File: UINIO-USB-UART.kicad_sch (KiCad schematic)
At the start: 32 parts, among them J1 Conn_01x08_Male, J2 Conn_01x04_Male, J3 Conn_01x07_Male, J4 Conn_01x06_Male, J5 Conn_01x04_Male, J6 Conn_01x07_Male, J7 Conn_01x03_Male, U1 CP2102, U2 CH343P

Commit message: Update PCB.
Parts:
- added R10, R7, R8, R9: 5.1K, Resistor_SMD:R_0603_1608Metric, symbol Device:R
- C3: value 0.1uF -> 4.7uF
- C4: value 4.7uF -> 0.1uF
- D1: value Green LED -> LED Red
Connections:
- net CH343_VDD_3.3V: now also J6.2 (Pin_2), R1.2; no longer J6.1 (Pin_1)
- net CH343_VDD_5V: now also J4.2 (Pin_2); no longer J4.1 (Pin_1), R1.2
- net CP2102_DTR: now also J2.1 (Pin_1); no longer J2.4 (Pin_4)
- net CP2102_RTS: now also J2.4 (Pin_4); no longer J2.1 (Pin_1)
- net CP2102_RXD: now also J2.2 (Pin_2); no longer J2.3 (Pin_3)
- net CP2102_TXD: now also J2.3 (Pin_3); no longer J2.2 (Pin_2)
- net CP2102_VDD_3.3V: now also J3.2 (Pin_2); no longer J3.1 (Pin_1)
- net CP2102_VDD_5V: now also J1.2 (Pin_2); no longer J1.1 (Pin_1)
- net GND: now also J1.1 (Pin_1), J3.1 (Pin_1), J4.1 (Pin_1), J6.1 (Pin_1), R10.1, R7.1, R8.1, R9.1; no longer J1.2 (Pin_2), J3.2 (Pin_2), J4.2 (Pin_2), J6.2 (Pin_2)
- net at USB2.A5 (CC1): now also R7.2
- net at USB2.B5 (CC2): now also R8.2
- net at USB1.A5 (CC1): now also R9.2
- net at USB1.B5 (CC2): now also R10.2
- no-connect marks 19 -> 15
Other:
- moved on the sheet: C6, D1, D4, F1, J2, R1, R4

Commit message: PCB Update.
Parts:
- D4: value Green LED -> LED Red
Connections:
- net CP2102_VDD_3.3V: now also R4.2
- net CP2102_VDD_5V: no longer R4.2
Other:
- moved on the sheet: C1, C2, C3, C4, D4, R4, U1

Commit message: Release UINIO-USB-UART version 3.0.0.
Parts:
- U2: footprint kicad_lceda:TQFN-16_L3.0-W3.0-P0.50-BL-EP1.7 -> Uinio:TQFN-16_L3.0-W3.0-P0.50-BL-EP1.7
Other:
- moved on the sheet: D1, R1
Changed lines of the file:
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@@
   (title_block
     (title "UINIO-USB-UART")
-    (date "2023-02-06")
+    (date "2023-02-07")
     (rev "Version 3.0.0")
     (company "电子技术博客 UinIO.com")
@@
     (stroke (width 0) (type default) (color 0 0 0 0))
   )
-  (wire (pts (xy 114.3 78.74) (xy 113.03 78.74))
+  (wire (pts (xy 114.3 76.2) (xy 113.03 76.2))
     (stroke (width 0) (type default) (color 0 0 0 0))
   )
@@
     (stroke (width 0.254) (type default) (color 0 0 0 0))
   )
-  (wire (pts (xy 121.92 69.85) (xy 121.92 66.04))
+  (wire (pts (xy 121.92 67.31) (xy 121.92 66.04))
     (stroke (width 0) (type default) (color 0 0 0 0))
   )
@@
     (stroke (width 0) (type default) (color 0 0 0 0))
   )
-  (wire (pts (xy 121.92 77.47) (xy 121.92 78.74))
+  (wire (pts (xy 121.92 74.93) (xy 121.92 76.2))
     (stroke (width 0) (type default) (color 0 0 0 0))
   )
@@
     (pin "2")
   )
-  (symbol (lib_id "Device:LED") (at 118.11 78.74 0) (unit 1)
-    (in_bom yes) (on_board yes)
-    (property "Reference" "D1" (id 0) (at 119.38 76.2 0)
-      (effects (font (size 1.27 1.27)) (justify right))
-    )
-    (property "Value" "LED Red" (id 1) (at 121.92 82.55 0)
-      (effects (font (size 1.27 1.27)) (justify right))
-    )
-    (property "Footprint" "LED_SMD:LED_0603_1608Metric" (id 2) (at 118.11 78.74 0)
-      (effects (font (size 1.27 1.27)) hide)
-    )
-    (property "Datasheet" "~" (id 3) (at 118.11 78.74 0)
+  (symbol (lib_id "Device:LED") (at 118.11 76.2 0) (unit 1)
+    (in_bom yes) (on_board yes)
+    (property "Reference" "D1" (id 0) (at 119.38 73.66 0)
+      (effects (font (size 1.27 1.27)) (justify right))
+    )
+    (property "Value" "LED Red" (id 1) (at 121.92 80.01 0)
+      (effects (font (size 1.27 1.27)) (justify right))
+    )
+    (property "Footprint" "LED_SMD:LED_0603_1608Metric" (id 2) (at 118.11 76.2 0)
+      (effects (font (size 1.27 1.27)) hide)
+    )
+    (property "Datasheet" "~" (id 3) (at 118.11 76.2 0)
       (effects (font (size 1.27 1.27)) hide)
     )
@@
     (pin "1")
   )
-  (symbol (lib_id "power:GND") (at 113.03 78.74 270) (mirror x) (unit 1)
-    (in_bom yes) (on_board yes)
-    (property "Reference" "#PWR02" (id 0) (at 106.68 78.74 0)
-      (effects (font (size 1.27 1.27)) hide)
-    )
-    (property "Value" "GND" (id 1) (at 110.49 78.74 90)
-      (effects (font (size 1.27 1.27)) (justify right))
-    )
-    (property "Footprint" "" (id 2) (at 113.03 78.74 0)
-      (effects (font (size 1.27 1.27)) hide)
-    )
-    (property "Datasheet" "" (id 3) (at 113.03 78.74 0)
-      (effects (font (size 1.27 1.27)) hide)
-    )
-    (pin "1")
-  )
-  (symbol (lib_id "Device:R") (at 121.92 73.66 0) (mirror x) (unit 1)
-    (in_bom yes) (on_board yes)
-    (property "Reference" "R1" (id 0) (at 124.46 73.66 90))
-    (property "Value" "2K" (id 1) (at 121.92 73.66 90))
-    (property "Footprint" "Resistor_SMD:R_0603_1608Metric" (id 2) (at 120.142 73.66 90)
-      (effects (font (size 1.27 1.27)) hide)
-    )
-    (property "Datasheet" "~" (id 3) (at 121.92 73.66 0)
+  (symbol (lib_id "power:GND") (at 113.03 76.2 270) (mirror x) (unit 1)
+    (in_bom yes) (on_board yes)
+    (property "Reference" "#PWR02" (id 0) (at 106.68 76.2 0)
+      (effects (font (size 1.27 1.27)) hide)
+    )
+    (property "Value" "GND" (id 1) (at 110.49 76.2 90)
+      (effects (font (size 1.27 1.27)) (justify right))
+    )
+    (property "Footprint" "" (id 2) (at 113.03 76.2 0)
+      (effects (font (size 1.27 1.27)) hide)
+    )
+    (property "Datasheet" "" (id 3) (at 113.03 76.2 0)
+      (effects (font (size 1.27 1.27)) hide)
+    )
+    (pin "1")
+  )
+  (symbol (lib_id "Device:R") (at 121.92 71.12 0) (mirror x) (unit 1)
+    (in_bom yes) (on_board yes)
+    (property "Reference" "R1" (id 0) (at 124.46 71.12 90))
+    (property "Value" "2K" (id 1) (at 121.92 71.12 90))
+    (property "Footprint" "Resistor_SMD:R_0603_1608Metric" (id 2) (at 120.142 71.12 90)
+      (effects (font (size 1.27 1.27)) hide)
+    )
+    (property "Datasheet" "~" (id 3) (at 121.92 71.12 0)
       (effects (font (size 1.27 1.27)) hide)
     )
@@
     (property "Reference" "U2" (id 0) (at 157.48 48.895 0))
     (property "Value" "CH343P" (id 1) (at 167.64 76.2 0))
-    (property "Footprint" "kicad_lceda:TQFN-16_L3.0-W3.0-P0.50-BL-EP1.7" (id 2) (at 170.18 76.2 0)
+    (property "Footprint" "Uinio:TQFN-16_L3.0-W3.0-P0.50-BL-EP1.7" (id 2) (at 170.18 76.2 0)
       (effects (font (size 1.27 1.27)) hide)
     )
@@
     )
     (path "/f9f0ec6d-076d-4cd3-8e74-63adeb9cbeee"
-      (reference "U2") (unit 1) (value "CH343P") (footprint "kicad_lceda:TQFN-16_L3.0-W3.0-P0.50-BL-EP1.7")
+      (reference "U2") (unit 1) (value "CH343P") (footprint "Uinio:TQFN-16_L3.0-W3.0-P0.50-BL-EP1.7")
     )
     (path "/89621895-1bc9-4914-8616-3f6600f3ea65"

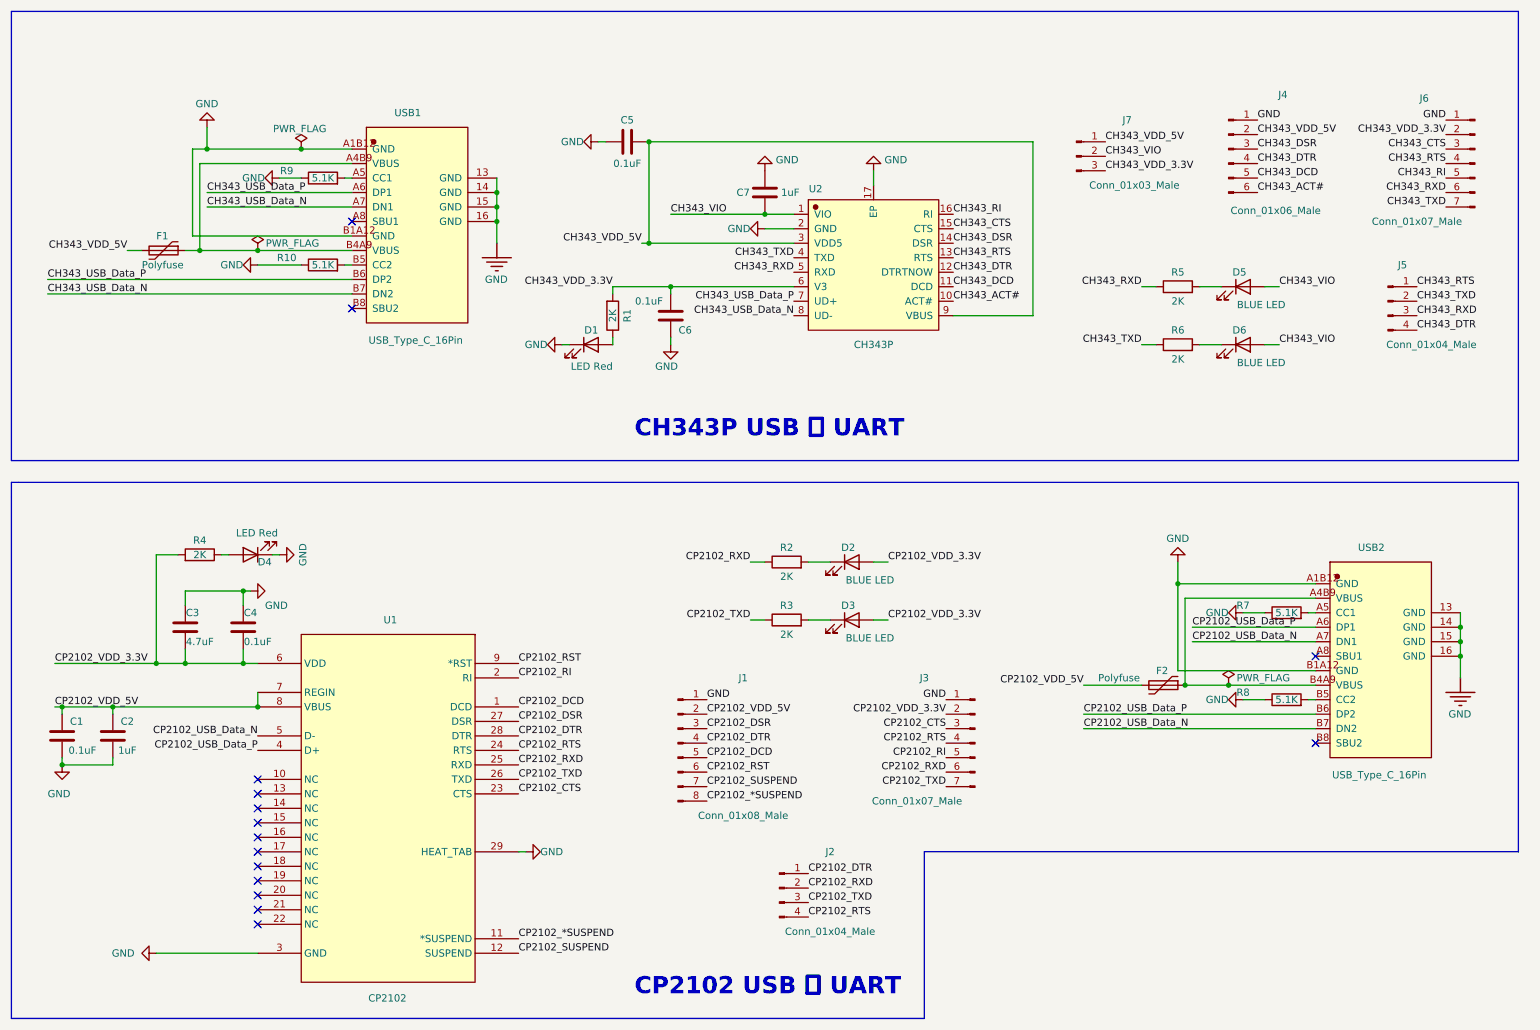
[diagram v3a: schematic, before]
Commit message: Prepare UINIO-USB-UART version 3.1.0
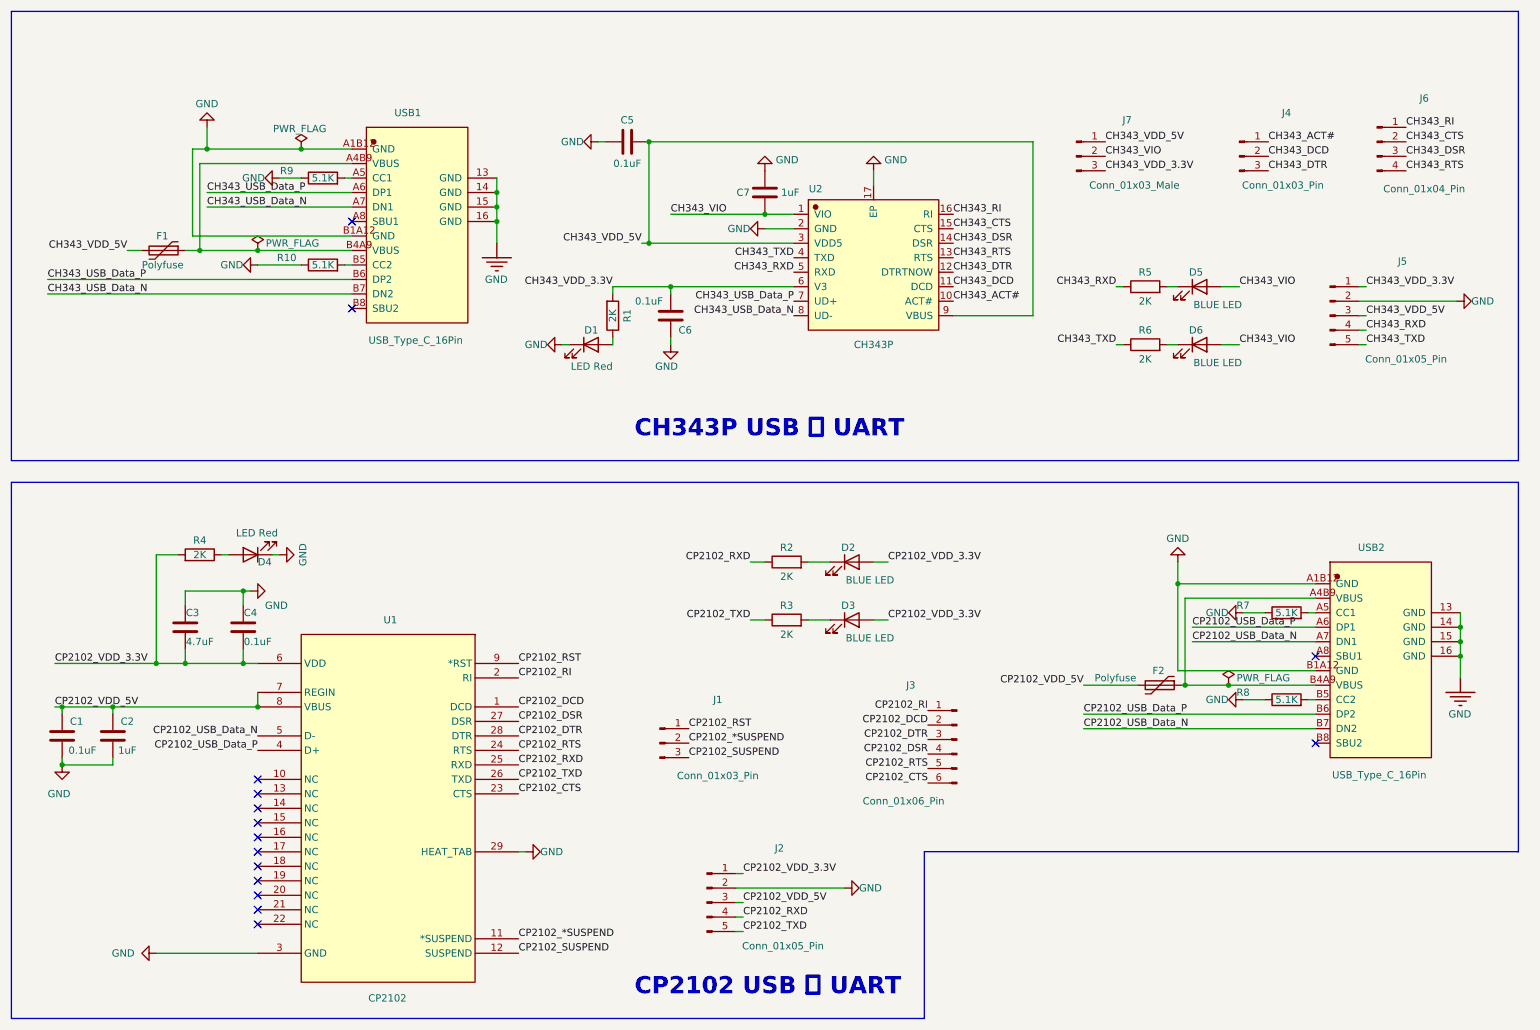
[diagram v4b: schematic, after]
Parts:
- removed J1: Conn_01x08_Male, Connector_PinHeader_2.54mm:PinHeader_1x08_P2.54mm_Vertical, symbol Connector:Conn_01x08_Male
- removed J2, J5: Conn_01x04_Male, Connector_PinHeader_2.54mm:PinHeader_1x04_P2.54mm_Vertical, symbol Connector:Conn_01x04_Male
- removed J3, J6: Conn_01x07_Male, Connector_PinHeader_2.54mm:PinHeader_1x07_P2.54mm_Vertical, symbol Connector:Conn_01x07_Male
- removed J4: Conn_01x06_Male, Connector_PinHeader_2.54mm:PinHeader_1x06_P2.54mm_Vertical, symbol Connector:Conn_01x06_Male
- added J1, J4: Conn_01x03_Pin, Connector_PinHeader_2.54mm:PinHeader_1x03_P2.54mm_Vertical, symbol Connector:Conn_01x03_Pin
- added J2, J5: Conn_01x05_Pin, Connector_PinHeader_2.54mm:PinHeader_1x05_P2.54mm_Vertical, symbol Connector:Conn_01x05_Pin
- added J3: Conn_01x06_Pin, Connector_PinHeader_2.54mm:PinHeader_1x06_P2.54mm_Vertical, symbol Connector:Conn_01x06_Pin
- added J6: Conn_01x04_Pin, Connector_PinHeader_2.54mm:PinHeader_1x04_P2.54mm_Vertical, symbol Connector:Conn_01x04_Pin
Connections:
- net CH343_ACT#: now also J4.1 (Pin_1)
- net CH343_CTS: now also J6.2 (Pin_2)
- net CH343_DCD: now also J4.2 (Pin_2)
- net CH343_DSR: now also J6.3 (Pin_3)
- net CH343_DTR: now also J4.3 (Pin_3)
- net CH343_RI: now also J6.1 (Pin_1)
- net CH343_RTS: now also J6.4 (Pin_4)
- net CH343_RXD: now also J5.4 (Pin_4)
- net CH343_TXD: now also J5.5 (Pin_5)
- net CH343_VDD_3.3V: now also J5.1 (Pin_1)
- net CH343_VDD_5V: now also J5.3 (Pin_3)
- net CP2102_*SUSPEND: now also J1.2 (Pin_2)
- net CP2102_CTS: now also J3.6 (Pin_6)
- net CP2102_DCD: now also J3.2 (Pin_2)
- net CP2102_DSR: now also J3.4 (Pin_4)
- net CP2102_DTR: now also J3.3 (Pin_3)
- net CP2102_RI: now also J3.1 (Pin_1)
- net CP2102_RST: now also J1.1 (Pin_1)
- net CP2102_RTS: now also J3.5 (Pin_5)
- net CP2102_RXD: now also J2.4 (Pin_4)
- net CP2102_SUSPEND: now also J1.3 (Pin_3)
- net CP2102_TXD: now also J2.5 (Pin_5)
- net CP2102_VDD_3.3V: now also J2.1 (Pin_1)
- net CP2102_VDD_5V: now also J2.3 (Pin_3)
- net GND: now also J2.2 (Pin_2), J5.2 (Pin_2)
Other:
- moved on the sheet: D5, D6, F2, R5, R6

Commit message: Prepare Version 3.2.0.
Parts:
- removed J7: Conn_01x03_Male, Connector_PinHeader_2.54mm:PinHeader_1x03_P2.54mm_Vertical, symbol Connector:Conn_01x03_Male
- added J7: Conn_01x03_Pin, Connector_PinHeader_2.54mm:PinHeader_1x03_P2.54mm_Vertical, symbol Connector:Conn_01x03_Pin
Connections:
- net CH343_RXD: now also J5.5 (Pin_5); no longer J5.4 (Pin_4)
- net CH343_TXD: now also J5.4 (Pin_4); no longer J5.5 (Pin_5)
- net CH343_VDD_3.3V: now also J5.3 (Pin_3), J7.3 (Pin_3); no longer J5.1 (Pin_1)
- net CH343_VDD_5V: now also J5.1 (Pin_1), J7.1 (Pin_1); no longer J5.3 (Pin_3)
- net CH343_VIO: now also J7.2 (Pin_2)
- net CP2102_VDD_3.3V: now also J2.3 (Pin_3); no longer J2.1 (Pin_1)
- net CP2102_VDD_5V: now also J2.1 (Pin_1); no longer J2.3 (Pin_3)
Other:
- moved on the sheet: F2, J1, J3, J4, J6, R5, R6

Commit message: Update PCB.
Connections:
- net CH343_VDD_3.3V: now also J7.1 (Pin_1); no longer J7.3 (Pin_3)
- net CH343_VDD_5V: now also J7.3 (Pin_3); no longer J7.1 (Pin_1)
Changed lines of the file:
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@@
     (effects (font (size 1.27 1.27)) (justify left bottom))
   )
-  (label "CH343_VDD_3.3V" (at 208.28 45.72 0) (fields_autoplaced)
+  (label "CH343_VDD_3.3V" (at 208.28 40.64 0) (fields_autoplaced)
     (effects (font (size 1.27 1.27)) (justify left bottom))
   )
@@
     (effects (font (size 1.27 1.27)) (justify left bottom))
   )
-  (label "CH343_VDD_5V" (at 208.28 40.64 0) (fields_autoplaced)
+  (label "CH343_VDD_5V" (at 208.28 45.72 0) (fields_autoplaced)
     (effects (font (size 1.27 1.27)) (justify left bottom))
   )

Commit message: Release UINIO-USB-UART version 3.2.0.
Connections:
- net CH343_VDD_3.3V: now also J5.2 (Pin_2); no longer J5.3 (Pin_3)
- net CP2102_VDD_3.3V: now also J2.2 (Pin_2); no longer J2.3 (Pin_3)
- net GND: now also J2.3 (Pin_3), J5.3 (Pin_3); no longer J2.2 (Pin_2), J5.2 (Pin_2)
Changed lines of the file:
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@@
   (title_block
     (title "UINIO-USB-UART")
-    (date "2023-06-26")
+    (date "2023-06-27")
     (rev "Version 3.2.0")
     (company "电子技术博客 UinIO.com")
@@
     (stroke (width 0) (type default))
   )
-  (wire (pts (xy 143.51 173.99) (xy 144.78 173.99))
+  (wire (pts (xy 143.51 171.45) (xy 144.78 171.45))
     (stroke (width 0) (type default))
   )
@@
     (stroke (width 0) (type default))
   )
-  (wire (pts (xy 252.73 68.58) (xy 270.51 68.58))
+  (wire (pts (xy 252.73 71.12) (xy 270.51 71.12))
     (stroke (width 0) (type default))
   )
@@
     (stroke (width 0) (type default))
   )
-  (wire (pts (xy 252.73 71.12) (xy 254 71.12))
+  (wire (pts (xy 252.73 68.58) (xy 254 68.58))
     (stroke (width 0) (type default))
   )
@@
     (stroke (width 0) (type default))
   )
-  (wire (pts (xy 143.51 171.45) (xy 162.56 171.45))
+  (wire (pts (xy 143.51 173.99) (xy 162.56 173.99))
     (stroke (width 0) (type default))
   )
@@
     (effects (font (size 1.27 1.27)) (justify left bottom))
   )
-  (label "CP2102_VDD_3.3V" (at 144.78 173.99 0) (fields_autoplaced)
-    (effects (font (size 1.27 1.27)) (justify left bottom))
-  )
-  (label "CH343_VDD_3.3V" (at 254 71.12 0) (fields_autoplaced)
+  (label "CP2102_VDD_3.3V" (at 144.78 171.45 0) (fields_autoplaced)
+    (effects (font (size 1.27 1.27)) (justify left bottom))
+  )
+  (label "CH343_VDD_3.3V" (at 254 68.58 0) (fields_autoplaced)
     (effects (font (size 1.27 1.27)) (justify left bottom))
   )
@@
     )
   )
-  (symbol (lib_id "power:GND") (at 162.56 171.45 90) (unit 1)
-    (in_bom yes) (on_board yes) (dnp no)
-    (property "Reference" "#PWR018" (at 168.91 171.45 0)
-      (effects (font (size 1.27 1.27)) hide)
-    )
-    (property "Value" "GND" (at 165.1 171.45 90)
-      (effects (font (size 1.27 1.27)) (justify right))
-    )
-    (property "Footprint" "" (at 162.56 171.45 0)
-      (effects (font (size 1.27 1.27)) hide)
-    )
-    (property "Datasheet" "" (at 162.56 171.45 0)
+  (symbol (lib_id "power:GND") (at 162.56 173.99 90) (unit 1)
+    (in_bom yes) (on_board yes) (dnp no)
+    (property "Reference" "#PWR018" (at 168.91 173.99 0)
+      (effects (font (size 1.27 1.27)) hide)
+    )
+    (property "Value" "GND" (at 165.1 173.99 90)
+      (effects (font (size 1.27 1.27)) (justify right))
+    )
+    (property "Footprint" "" (at 162.56 173.99 0)
+      (effects (font (size 1.27 1.27)) hide)
+    )
+    (property "Datasheet" "" (at 162.56 173.99 0)
       (effects (font (size 1.27 1.27)) hide)
     )
@@
     )
   )
-  (symbol (lib_id "power:GND") (at 270.51 68.58 90) (unit 1)
-    (in_bom yes) (on_board yes) (dnp no)
-    (property "Reference" "#PWR019" (at 276.86 68.58 0)
-      (effects (font (size 1.27 1.27)) hide)
-    )
-    (property "Value" "GND" (at 273.05 68.58 90)
-      (effects (font (size 1.27 1.27)) (justify right))
-    )
-    (property "Footprint" "" (at 270.51 68.58 0)
-      (effects (font (size 1.27 1.27)) hide)
-    )
-    (property "Datasheet" "" (at 270.51 68.58 0)
-      (effects (font (size 1.27 1.27)) hide)
-    )
+  (symbol (lib_id "power:GND") (at 270.51 71.12 90) (unit 1)
+    (in_bom yes) (on_board yes) (dnp no)
+    (property "Reference" "#PWR019" (at 276.86 71.12 0)
+      (effects (font (size 1.27 1.27)) hide)
+    )
+    (property "Value" "GND" (at 273.05 71.12 90)
+      (effects (font (size 1.27 1.27)) (justify right))
+    )
+    (property "Footprint" "" (at 270.51 71.12 0)
+      (effects (font (size 1.27 1.27)) hide)
+    )
+    (property "Datasheet" "" (at 270.51 71.12 0)
+      (effects (font (size 1.27 1.27)) hide)
+    )

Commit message: Release UINIO-USB-UART version 3.2.1.
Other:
- company: 电子技术博客 UinIO.com -> UinIO.com 电子技术实验室
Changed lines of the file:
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@@
   (title_block
     (title "UINIO-USB-UART")
-    (date "2023-06-27")
-    (rev "Version 3.2.0")
-    (company "电子技术博客 UinIO.com")
+    (date "2024-01-10")
+    (rev "Version 3.2.1")
+    (company "UinIO.com 电子技术实验室")
   )
   (junction (at 148.59 53.34) (diameter 0) (color 0 0 0 0)
